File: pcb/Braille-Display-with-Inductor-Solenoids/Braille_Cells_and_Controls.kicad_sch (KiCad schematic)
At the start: 1 part, among them U26 74HC595

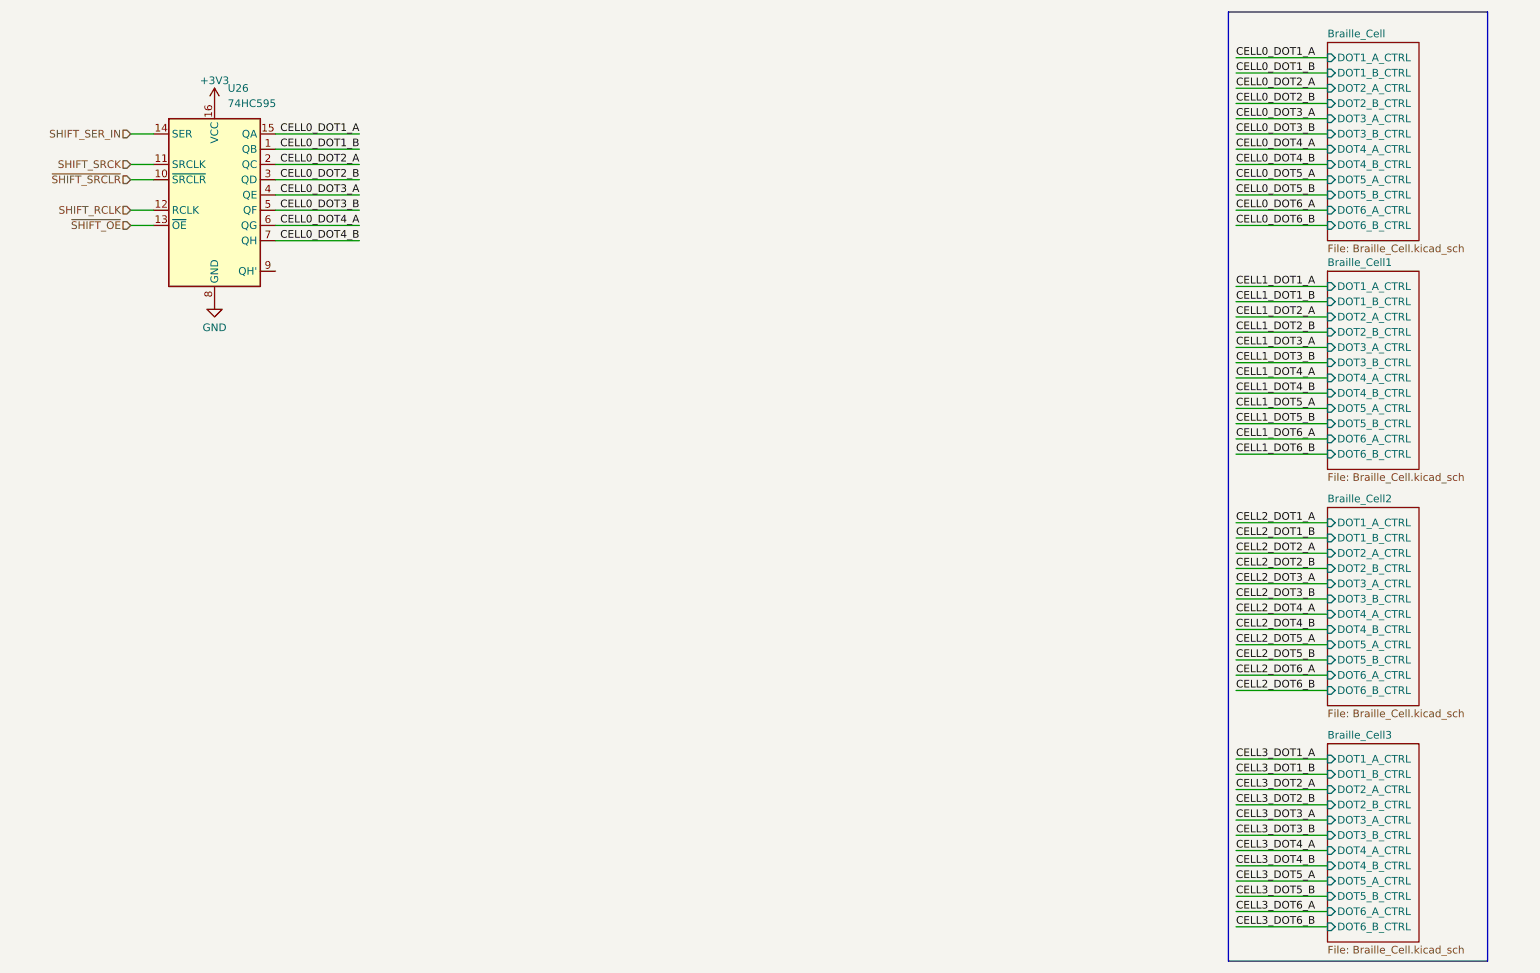
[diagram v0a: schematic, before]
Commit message: Layout debugging components
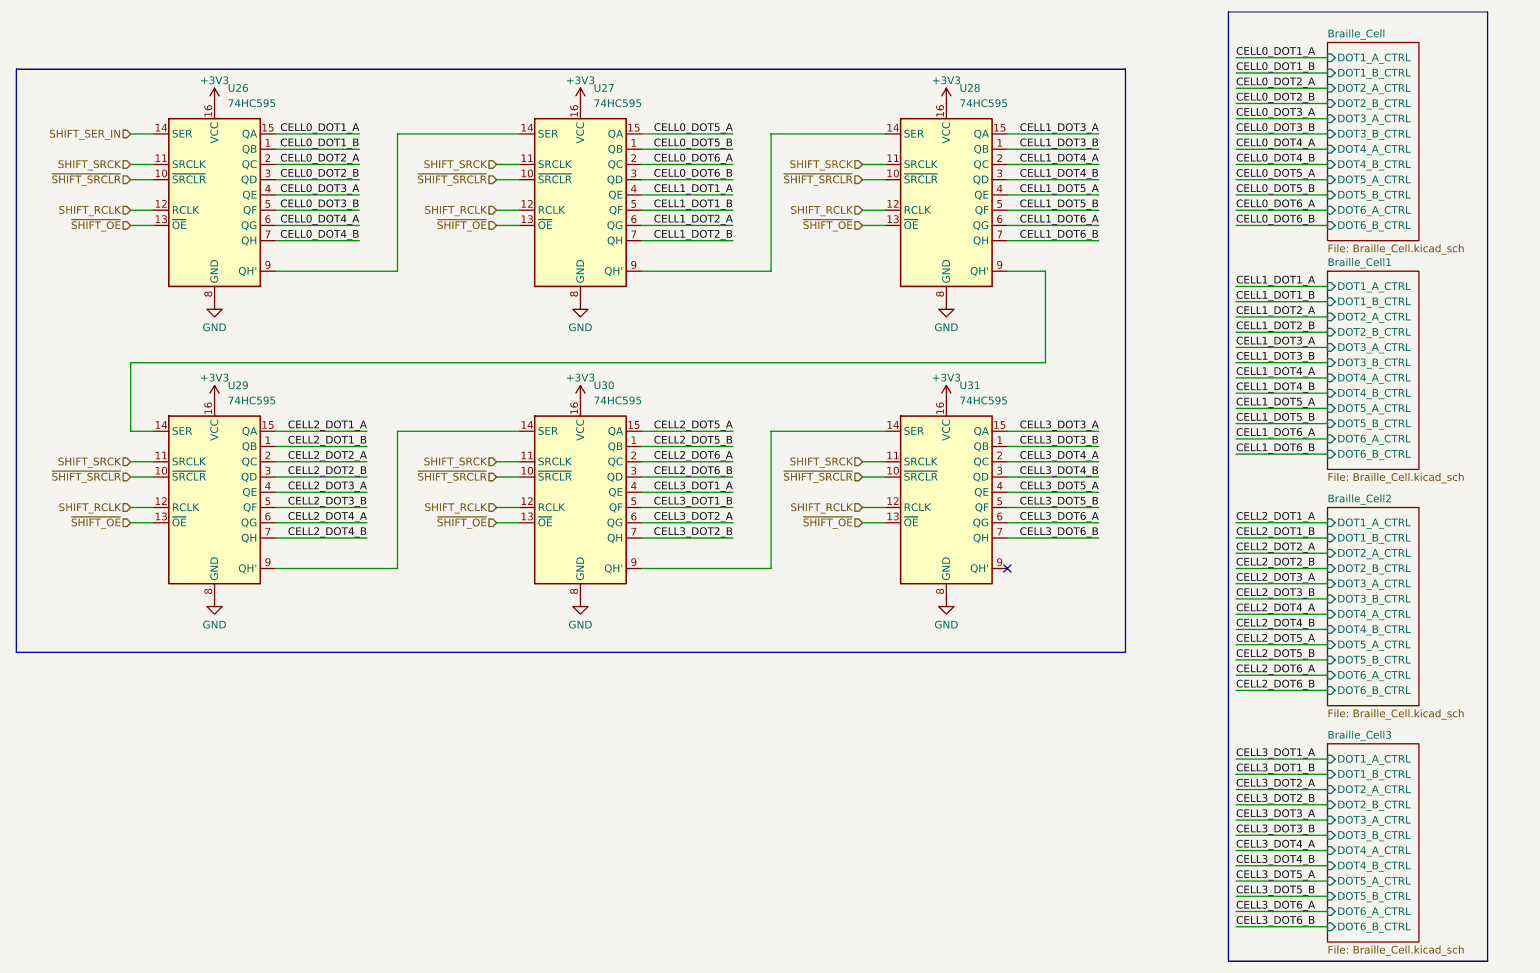
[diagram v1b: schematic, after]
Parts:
- added U27, U28, U29, U30, U31: 74HC595, Package_SO:SOP-16_3.9x9.9mm_P1.27mm, symbol 74xx:74HC595
- U26: footprint (none) -> Package_SO:SOP-16_3.9x9.9mm_P1.27mm
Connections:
- net +3V3: now also U27.16 (VCC), U28.16 (VCC), U29.16 (VCC), U30.16 (VCC), U31.16 (VCC)
- net CELL0_DOT5_A: now also U27.15 (QA)
- net CELL0_DOT5_B: now also U27.1 (QB)
- net CELL0_DOT6_A: now also U27.2 (QC)
- net CELL0_DOT6_B: now also U27.3 (QD)
- net CELL1_DOT1_A: now also U27.4 (QE)
- net CELL1_DOT1_B: now also U27.5 (QF)
- net CELL1_DOT2_A: now also U27.6 (QG)
- net CELL1_DOT2_B: now also U27.7 (QH)
- net CELL1_DOT3_A: now also U28.15 (QA)
- net CELL1_DOT3_B: now also U28.1 (QB)
- net CELL1_DOT4_A: now also U28.2 (QC)
- net CELL1_DOT4_B: now also U28.3 (QD)
- net CELL1_DOT5_A: now also U28.4 (QE)
- net CELL1_DOT5_B: now also U28.5 (QF)
- net CELL1_DOT6_A: now also U28.6 (QG)
- net CELL1_DOT6_B: now also U28.7 (QH)
- net CELL2_DOT1_A: now also U29.15 (QA)
- net CELL2_DOT1_B: now also U29.1 (QB)
- net CELL2_DOT2_A: now also U29.2 (QC)
- net CELL2_DOT2_B: now also U29.3 (QD)
- net CELL2_DOT3_A: now also U29.4 (QE)
- net CELL2_DOT3_B: now also U29.5 (QF)
- net CELL2_DOT4_A: now also U29.6 (QG)
- net CELL2_DOT4_B: now also U29.7 (QH)
- net CELL2_DOT5_A: now also U30.15 (QA)
- net CELL2_DOT5_B: now also U30.1 (QB)
- net CELL2_DOT6_A: now also U30.2 (QC)
- net CELL2_DOT6_B: now also U30.3 (QD)
- net CELL3_DOT1_A: now also U30.4 (QE)
- net CELL3_DOT1_B: now also U30.5 (QF)
- net CELL3_DOT2_A: now also U30.6 (QG)
- net CELL3_DOT2_B: now also U30.7 (QH)
- net CELL3_DOT3_A: now also U31.15 (QA)
- net CELL3_DOT3_B: now also U31.1 (QB)
- net CELL3_DOT4_A: now also U31.2 (QC)
- net CELL3_DOT4_B: now also U31.3 (QD)
- net CELL3_DOT5_A: now also U31.4 (QE)
- net CELL3_DOT5_B: now also U31.5 (QF)
- net CELL3_DOT6_A: now also U31.6 (QG)
- net CELL3_DOT6_B: now also U31.7 (QH)
- net GND: now also U27.8 (GND), U28.8 (GND), U29.8 (GND), U30.8 (GND), U31.8 (GND)
- net SHIFT_RCLK: now also U27.12 (RCLK), U28.12 (RCLK), U29.12 (RCLK), U30.12 (RCLK), U31.12 (RCLK)
- net SHIFT_SRCK: now also U27.11 (SRCLK), U28.11 (SRCLK), U29.11 (SRCLK), U30.11 (SRCLK), U31.11 (SRCLK)
- net ~{SHIFT_OE}: now also U27.13 (~{OE}), U28.13 (~{OE}), U29.13 (~{OE}), U30.13 (~{OE}), U31.13 (~{OE})
- net ~{SHIFT_SRCLR}: now also U27.10 (~{SRCLR}), U28.10 (~{SRCLR}), U29.10 (~{SRCLR}), U30.10 (~{SRCLR}), U31.10 (~{SRCLR})
- net at U26.9 (QH'): now also U27.14 (SER)
- new net: U28.9 (QH'), U29.14 (SER)
- new net: U29.9 (QH'), U30.14 (SER)
- new net: U30.9 (QH'), U31.14 (SER)
- new net: U27.9 (QH'), U28.14 (SER)
- no-connect marks 0 -> 1
